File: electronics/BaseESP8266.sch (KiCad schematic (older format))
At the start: 17 parts, among them P1 CONN_01X09, P2 CONN_01X09, SW1 Reset, T1 CONN_01X01, T2 CONN_01X01, U1 ESP-13-WROOM-02

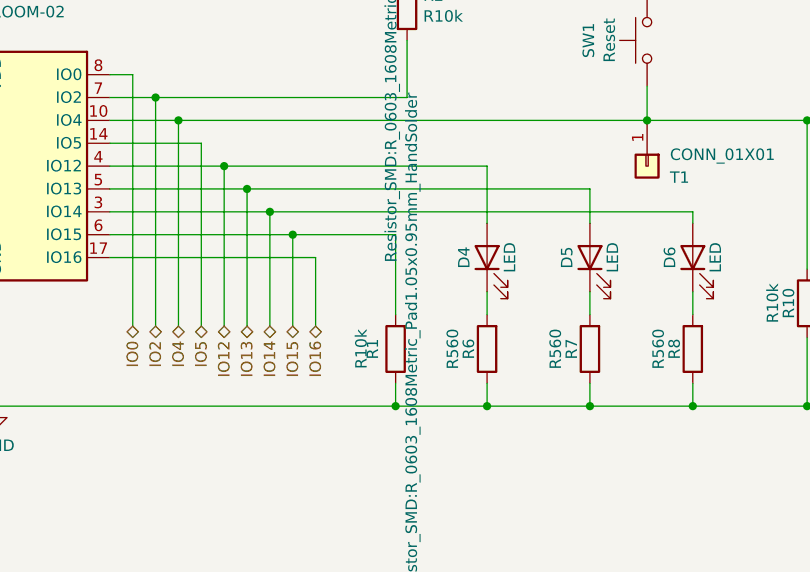
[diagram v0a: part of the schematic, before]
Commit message: Changed switch, finished laying out PCB.
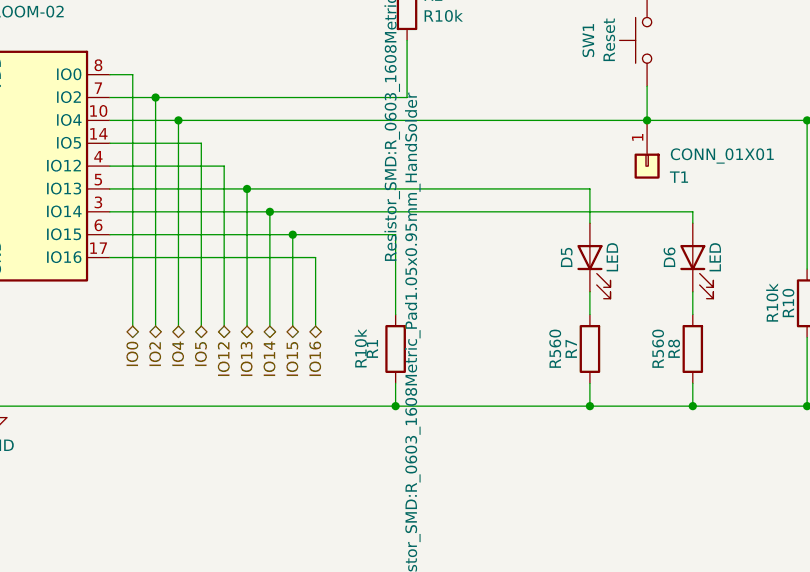
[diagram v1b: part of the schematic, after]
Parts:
- removed D4: LED, LED_SMD:LED_0805_2012Metric_Pad1.15x1.40mm_HandSolder, symbol Device:LED
- removed R6: R560, Resistor_SMD:R_0603_1608Metric_Pad1.05x0.95mm_HandSolder, symbol Device:R
- D5, D6: footprint LED_SMD:LED_0805_2012Metric_Pad1.15x1.40mm_HandSolder -> mcqn-kicad-lib:LED_SMD_WL-SMSW_side-emitting; Farnell 2290332 -> 2322102; Farnell Price/Stock https://uk.farnell.com/kingbright/kp-2012seck/led-0805-250m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 -> https://uk.farnell.com/wurth-elektronik/155124vs73200/led-1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
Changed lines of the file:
@@
 $EndDescr
-Wire Wire Line
-	8900 3750 8900 3850
 Wire Wire Line
 	9350 3750 9350 3850
@@
 $EndComp
 $Comp
-L Device:R R?
-U 1 1 5F9FDA48
-P 8900 4000
-AR Path="/5F9FDA48" Ref="R?"  Part="1"
-AR Path="/5F935E83/5F9FDA48" Ref="R6"  Part="1"
-AR Path="/5F8DAD46/5F9FDA48" Ref="R6"  Part="1"
-F 0 "R6" V 8980 4000 50  0000 C CNN
-F 1 "R560" V 9050 4000 50  0000 C CNN
-F 2 "Resistor_SMD:R_0603_1608Metric_Pad1.05x0.95mm_HandSolder" V 8830 4000 50  0001 C CNN
-F 3 "" H 8900 4000 50  0000 C CNN
-F 4 "2502470" V 8900 4000 50  0001 C CNN "Farnell"
-F 5 "https://uk.farnell.com/walsin/wr06x5600ftl/res-560r-1-75v-0603-thick-film/dp/2502470" V 8900 4000 50  0001 C CNN "Farnell Price/Stock"
-	1    8900 4000
-	-1   0    0    1
-$EndComp
-$Comp
 L Device:LED D?
 U 1 1 5F9FDA4E
@@
 F 0 "D6" H 9800 3700 50  0000 C CNN
 F 1 "LED" H 9800 3500 50  0000 C CNN
-F 2 "LED_SMD:LED_0805_2012Metric_Pad1.15x1.40mm_HandSolder" H 9800 3600 50  0001 C CNN
+F 2 "mcqn-kicad-lib:LED_SMD_WL-SMSW_side-emitting" H 9800 3600 50  0001 C CNN
 F 3 "" H 9800 3600 50  0000 C CNN
-F 4 "2290332" H 9800 3600 50  0001 C CNN "Farnell"
-F 5 "https://uk.farnell.com/kingbright/kp-2012seck/led-0805-250mcd-orange/dp/2290332" H 9800 3600 50  0001 C CNN "Farnell Price/Stock"
+F 4 "2322102" H 9800 3600 50  0001 C CNN "Farnell"
+F 5 "https://uk.farnell.com/wurth-elektronik/155124vs73200/led-1204-b-green-50mcd-573nm/dp/2322102" H 9800 3600 50  0001 C CNN "Farnell Price/Stock"
 	1    9800 3600
 	0    -1   -1   0
@@
 F 0 "D5" H 9350 3700 50  0000 C CNN
 F 1 "LED" H 9350 3500 50  0000 C CNN
-F 2 "LED_SMD:LED_0805_2012Metric_Pad1.15x1.40mm_HandSolder" H 9350 3600 50  0001 C CNN
+F 2 "mcqn-kicad-lib:LED_SMD_WL-SMSW_side-emitting" H 9350 3600 50  0001 C CNN
 F 3 "" H 9350 3600 50  0000 C CNN
-F 4 "2290332" H 9350 3600 50  0001 C CNN "Farnell"
-F 5 "https://uk.farnell.com/kingbright/kp-2012seck/led-0805-250mcd-orange/dp/2290332" H 9350 3600 50  0001 C CNN "Farnell Price/Stock"
+F 4 "2322102" H 9350 3600 50  0001 C CNN "Farnell"
+F 5 "https://uk.farnell.com/wurth-elektronik/155124vs73200/led-1204-b-green-50mcd-573nm/dp/2322102" H 9350 3600 50  0001 C CNN "Farnell Price/Stock"
 	1    9350 3600
-	0    -1   -1   0
-$EndComp
-$Comp
-L Device:LED D?
-U 1 1 5F9FDA5A
-P 8900 3600
-AR Path="/5F9FDA5A" Ref="D?"  Part="1"
-AR Path="/5F935E83/5F9FDA5A" Ref="D4"  Part="1"
-AR Path="/5F8DAD46/5F9FDA5A" Ref="D4"  Part="1"
-F 0 "D4" H 8900 3700 50  0000 C CNN
-F 1 "LED" H 8900 3500 50  0000 C CNN
-F 2 "LED_SMD:LED_0805_2012Metric_Pad1.15x1.40mm_HandSolder" H 8900 3600 50  0001 C CNN
-F 3 "" H 8900 3600 50  0000 C CNN
-F 4 "2290332" H 8900 3600 50  0001 C CNN "Farnell"
-F 5 "https://uk.farnell.com/kingbright/kp-2012seck/led-0805-250mcd-orange/dp/2290332" H 8900 3600 50  0001 C CNN "Farnell Price/Stock"
-	1    8900 3600
 	0    -1   -1   0
 $EndComp
@@
 $EndComp
 Wire Wire Line
-	8900 3200 8900 3450
-Wire Wire Line
 	9350 3300 9350 3450
 Wire Wire Line
@@
 Wire Wire Line
 	6750 3800 6750 4250
-Wire Wire Line
-	8900 4150 8900 4250
-Wire Wire Line
-	8900 4250 8500 4250
 Connection ~ 6750 4250
 Wire Wire Line
 	9350 4150 9350 4250
-Wire Wire Line
-	9350 4250 8900 4250
-Connection ~ 8900 4250
 Wire Wire Line
 	9800 4150 9800 4250
@@
 Wire Wire Line
 	7750 3900 7750 3200
-Connection ~ 7750 3200
-Wire Wire Line
-	7750 3200 8900 3200
 Wire Wire Line
 	7850 3900 7850 3300
-Connection ~ 7850 3300
-Wire Wire Line
-	7850 3300 9350 3300
 Wire Wire Line
 	7950 3900 7950 3400
@@
 Wire Wire Line
 	8150 3600 7250 3600
+Wire Wire Line
+	8500 4250 9350 4250
+Connection ~ 7850 3300
+Wire Wire Line
+	7850 3300 9350 3300
 $EndSCHEMATC
